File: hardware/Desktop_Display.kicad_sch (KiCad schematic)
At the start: 3 parts, among them J1 Conn_01x02, J2 Barrel_Jack_Switch_MountingPin, U1 ESP32-DevKitC

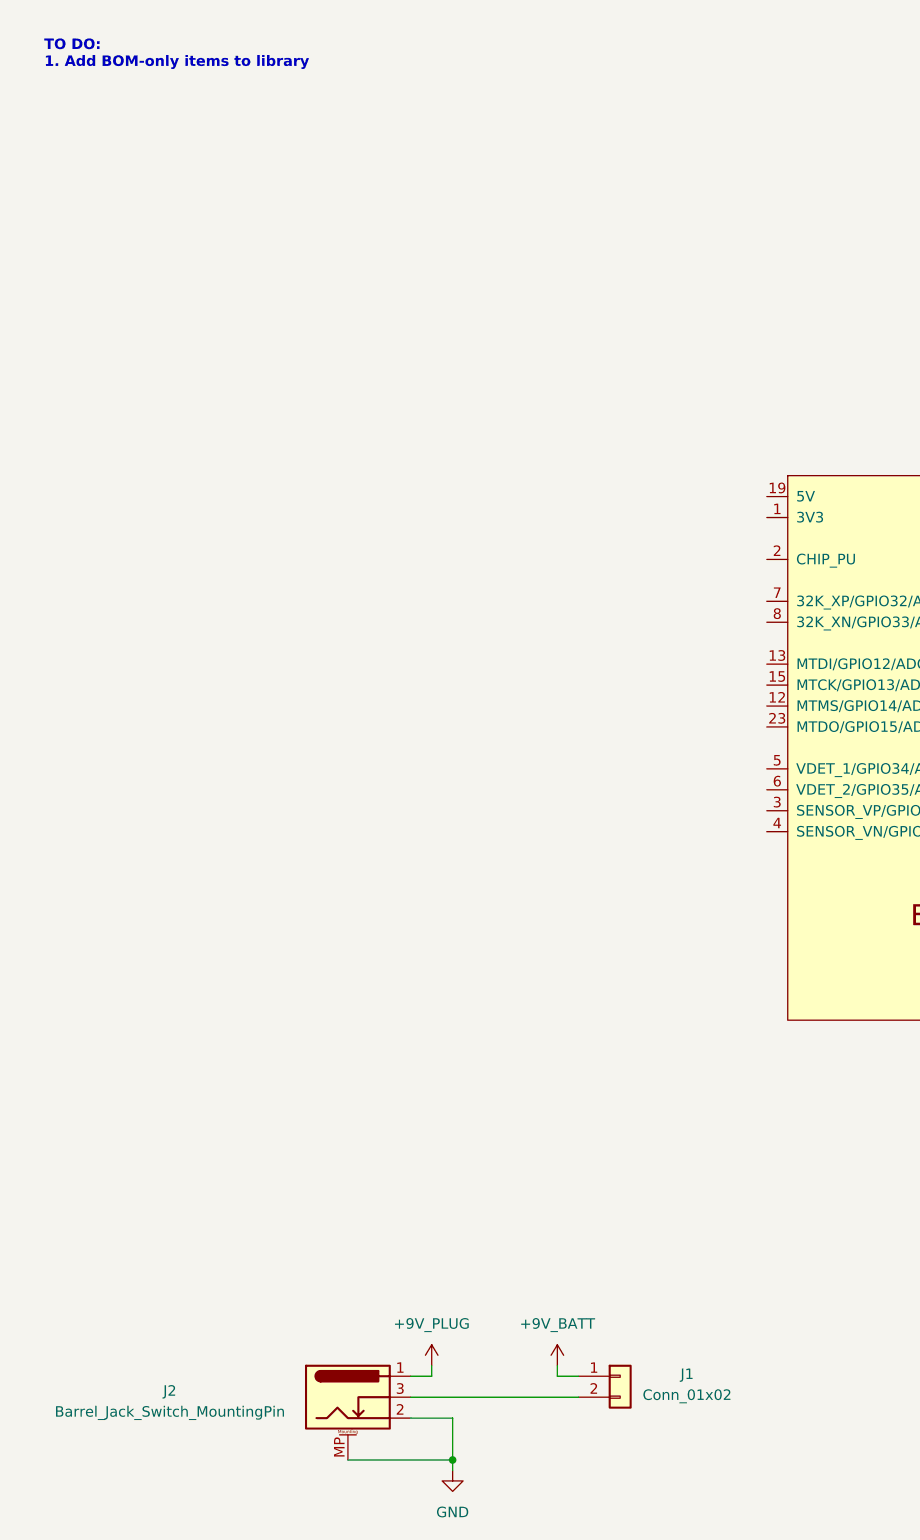
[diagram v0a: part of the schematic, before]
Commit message: Added generic LDO, more instructions, diode OR for power, and LEDs for power use indication.
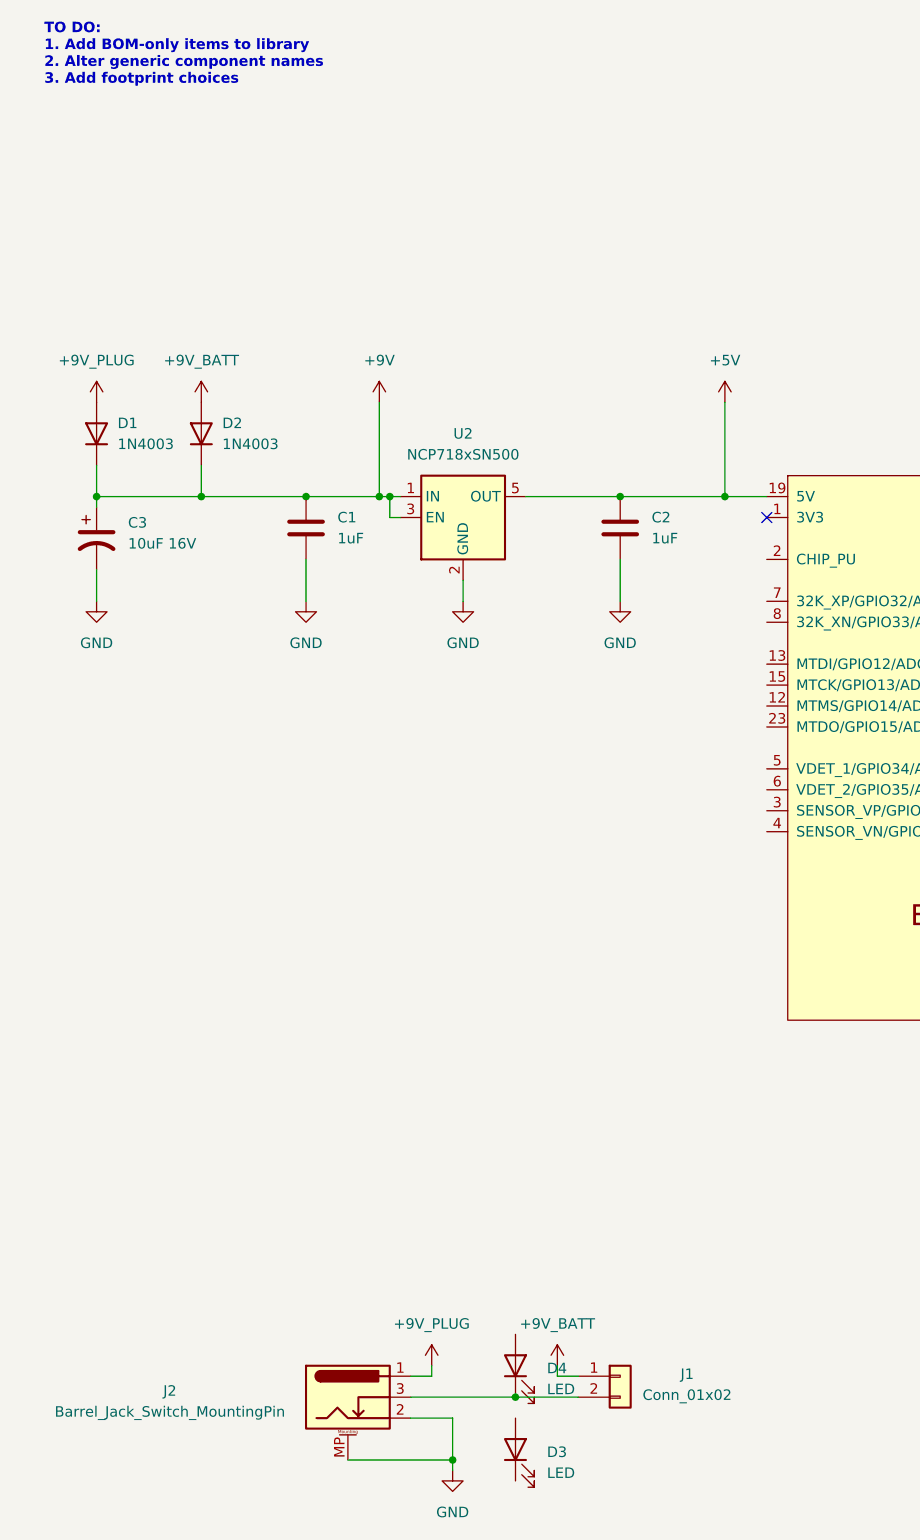
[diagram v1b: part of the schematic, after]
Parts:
- added C1, C2: 1uF, symbol Device:C
- added C3: 10uF 16V, symbol Device:C_Polarized_US
- added D1, D2: 1N4003, Diode_THT:D_DO-41_SOD81_P10.16mm_Horizontal, symbol Diode:1N4003
- added D3, D4: LED, symbol Device:LED
- added U2: NCP718xSN500, Package_TO_SOT_SMD:SOT-23-5, symbol Regulator_Linear:NCP718xSN500
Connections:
- net +9V_BATT: now also D2.2 (A)
- net +9V_PLUG: now also D1.2 (A)
- net GND: now also C1.2, C2.2, C3.2, U2.2 (GND)
- net +5V: now reaches U1.19 (5V)
- net +5V: now also C2.1, U2.5 (OUT)
- net at J1.2 (Pin_2), J2.3: now also D4.1 (K)
- new net +9V: C1.1, C3.1, D1.1 (K), D2.1 (K), U2.1 (IN), U2.3 (EN)
- no-connect marks 0 -> 1
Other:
- note added: "TO DO: 1. Add BOM-only items to library 2. Alter generic component names 3. Add footprint choices"
- note removed: "TO DO: 1. Add BOM-only items to library"

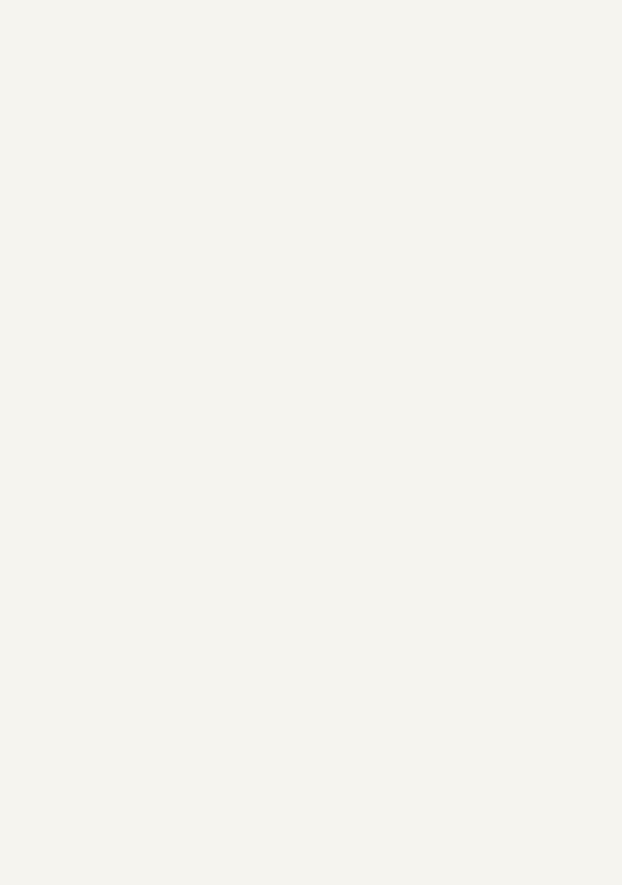
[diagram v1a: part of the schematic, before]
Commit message: Added mounting holes and a 10M ESD resistor between chassis and GND.
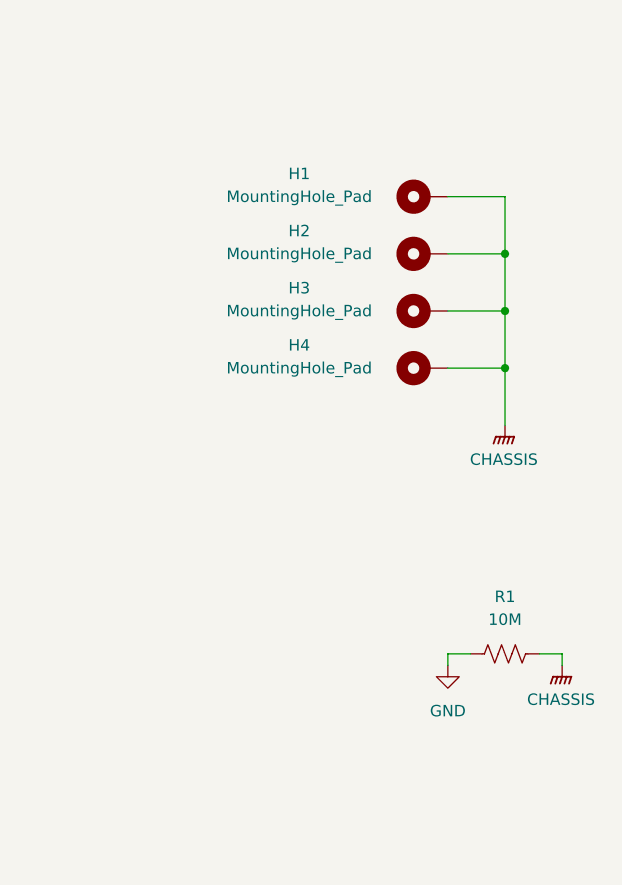
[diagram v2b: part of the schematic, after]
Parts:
- added H1, H2, H3, H4: MountingHole_Pad, symbol Mechanical:MountingHole_Pad
- added R1: 10M, symbol Device:R_US
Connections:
- net GND: now also R1.1
- new net CHASSIS: H1.1, H2.1, H3.1, H4.1, R1.2
